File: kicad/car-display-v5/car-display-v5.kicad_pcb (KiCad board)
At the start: 4 copper layers, 35.8 x 35.8 mm, 52 parts, among them J1 AVRISP-6, J2 Screw_Terminal_01x03, J3 PicoBlade F 1x7, J4 Socket 1x6 0.1", J5 JMP 1x3 0.05", U1 ATmega328PB-M, U2 TXS0108ERGYR, U3 MCP25625T-E/ML, U4 TPSM365R3RDNR, U5 LP3988*-*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

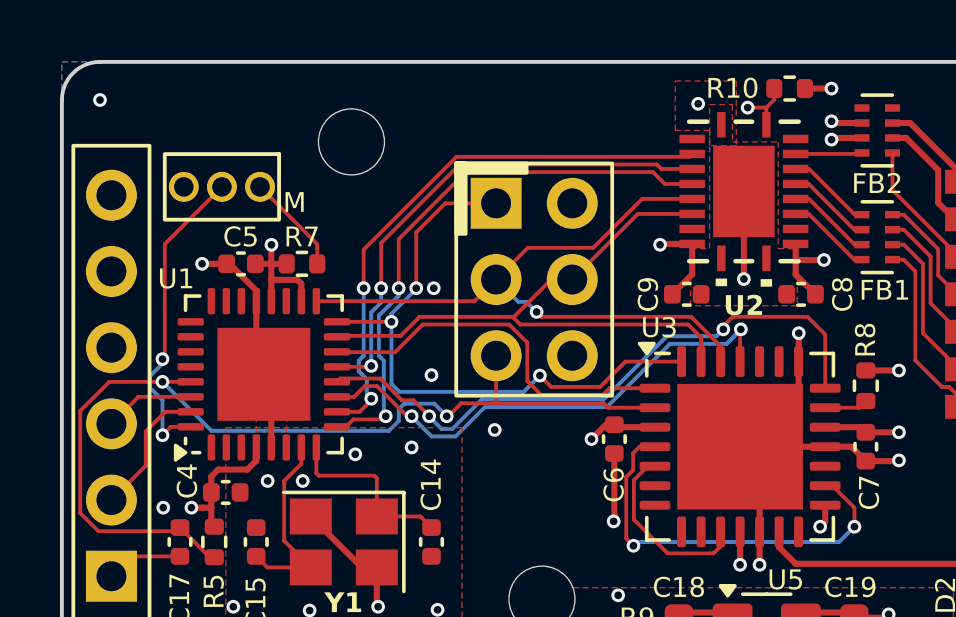
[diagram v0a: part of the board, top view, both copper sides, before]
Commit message: Add 3.3V PGOOD trace
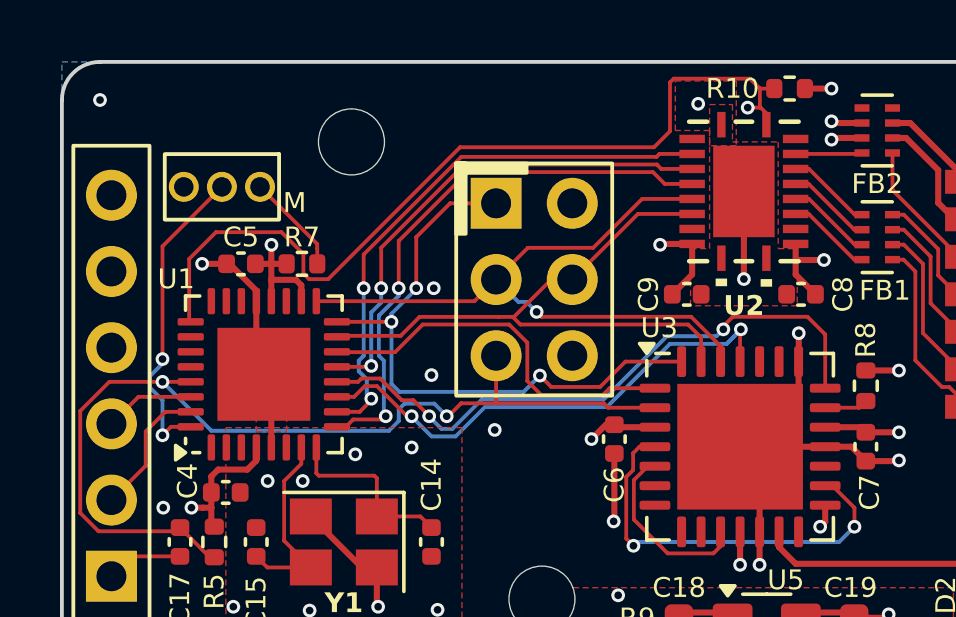
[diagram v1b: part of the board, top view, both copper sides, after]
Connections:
- U1 pad 25: unconnected-(U1-PC2-Pad25) -> PG_3V3
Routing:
- net PG_3V3: track 31.8 -> 58.4 mm

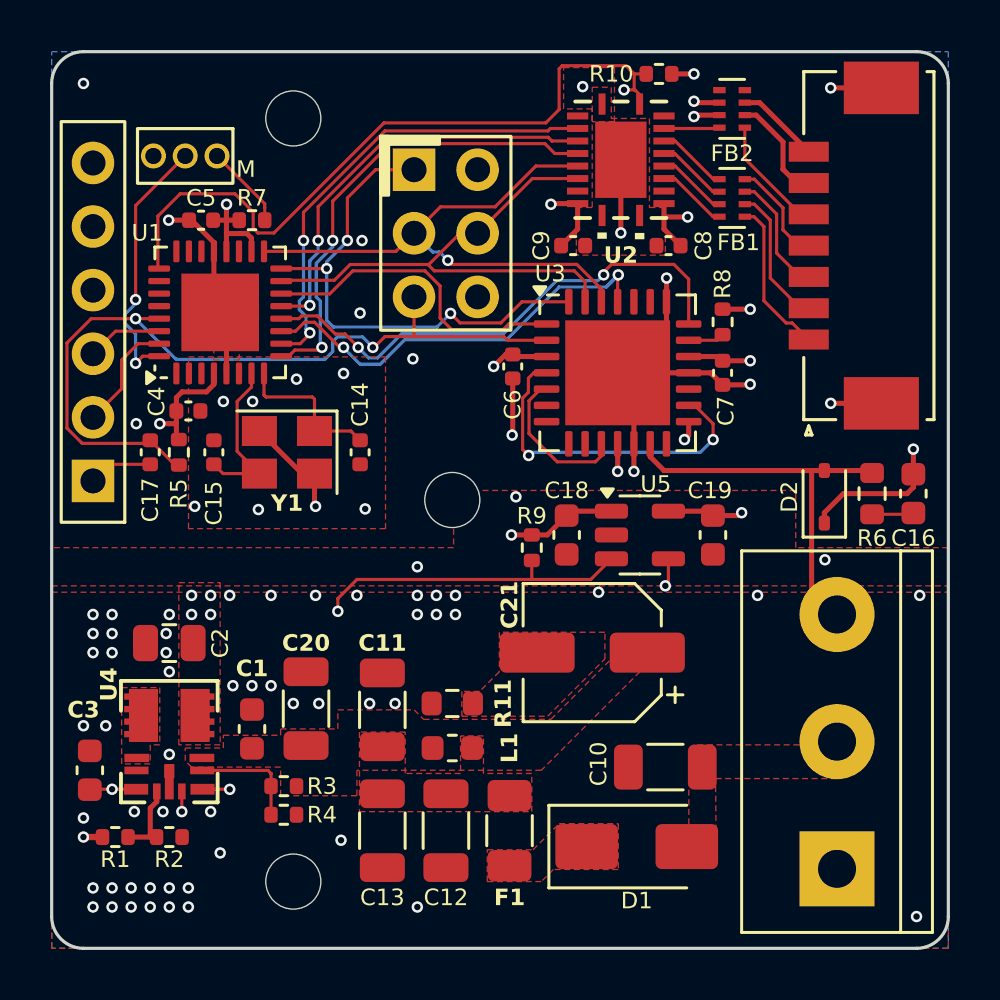
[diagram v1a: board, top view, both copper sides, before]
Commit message: Modify 3.3V trace
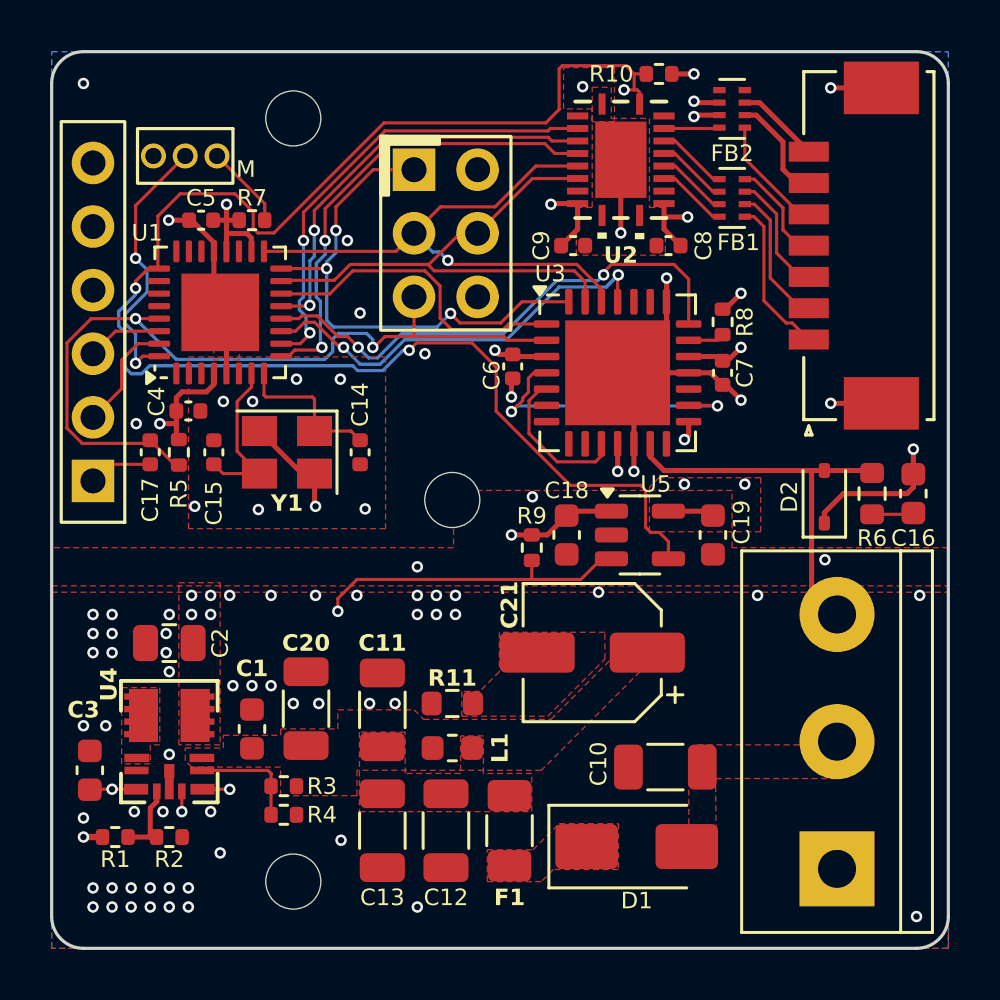
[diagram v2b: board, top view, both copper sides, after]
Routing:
- net PG_3V3: track 58.4 -> 62.0 mm, vias 2 -> 3
- net GND: track 43.9 -> 42.2 mm
- net T_{X}CAN: track 13.6 -> 11.9 mm
- net +3.3V: track 7.87 -> 6.67 mm, vias 4 -> 5
- added copper zone on F.Cu, net +3.3V

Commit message: Move OLED connector to side opposite of CAN input
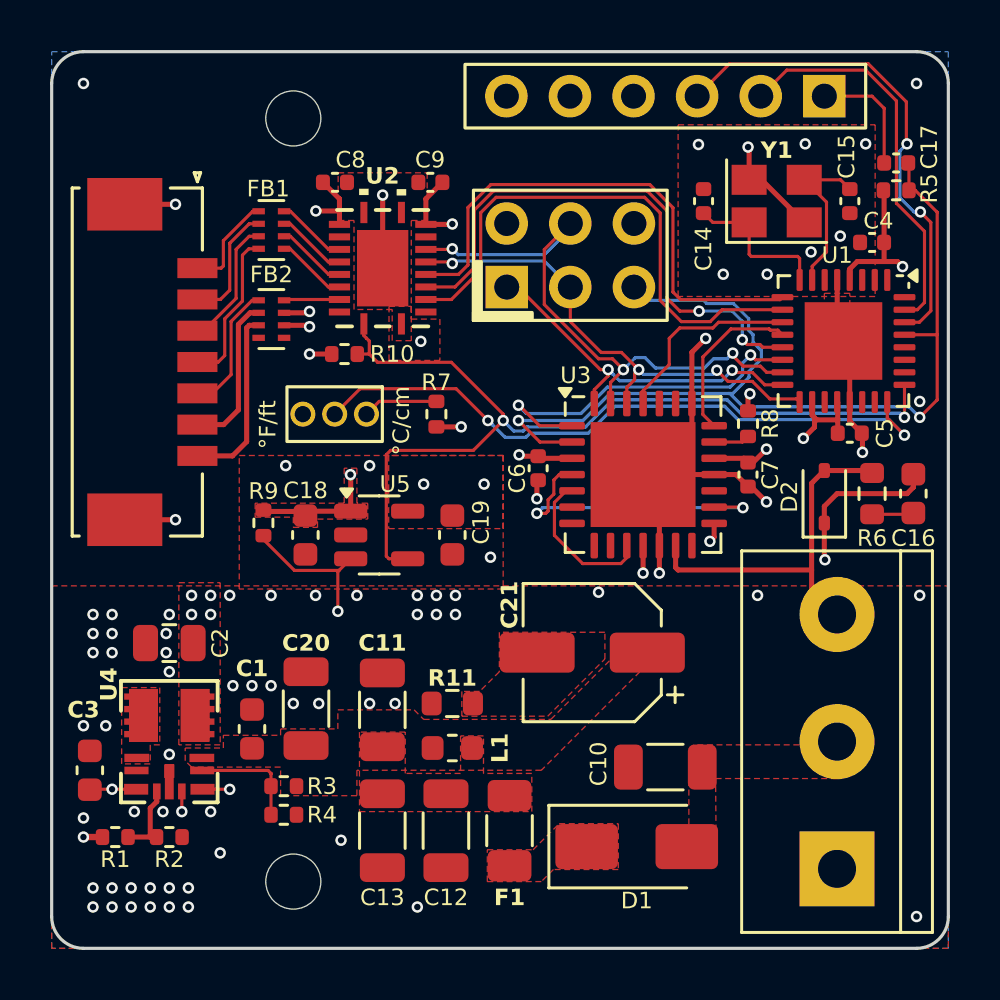
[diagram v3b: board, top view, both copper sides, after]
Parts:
- removed H3: MountingHole_Pad, MountingHole:MountingHole_2.2mm_M2_DIN965
- moved J4 33.0 mm to (143.6, 154.2), turned to -90 degrees
- moved C17 32.0 mm to (146.5, 156.8), turned to 180 degrees
- moved R5 30.5 mm to (146.5, 157.9), turned to 0 degrees
- moved C4 28.1 mm to (145.5, 160.0), turned to 180 degrees
- moved C15 27.3 mm to (144.7, 158.4), turned to -90 degrees
- moved C5 27.3 mm to (144.7, 167.6), turned to 0 degrees
- moved U1 24.9 mm to (144.4, 164.0), turned to -90 degrees
- moved J3 24.6 mm to (118.6, 161.0), turned to -90 degrees
- moved Y1 22.0 mm to (141.7, 158.4), turned to 0 degrees
- moved FB2 20.2 mm to (121.6, 163.1), turned to -90 degrees
- moved FB1 18.4 mm to (121.6, 159.5), turned to -90 degrees
- moved C14 17.0 mm to (138.8, 158.4), turned to 90 degrees
- moved R10 16.8 mm to (124.5, 164.5), turned to 0 degrees
- moved C8 13.6 mm to (124.1, 157.6), turned to 0 degrees
- moved J5 11.9 mm to (124.1, 166.9)
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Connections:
- net /OSC+ renamed OSC+
- net /OSC- renamed OSC-
- U1 pad 24: unconnected-(U1-PC1-Pad24) -> SEL_UNIT
- U1 pad 32: SEL_UNIT -> unconnected-(U1-PD2-Pad32)
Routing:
- net PG_3V3: track 62.0 -> 36.9 mm, vias 3 -> 2
- net FTDI_RX: track 3.02 -> 19.9 mm, vias 0 -> 2
- net SEL_UNIT: track 10.9 -> 26.6 mm
- net CLK: track 20.7 -> 6.67 mm, vias 2 -> 0
- net FTDI_TX: track 4.53 -> 15.8 mm
- net INT_CAN: track 17.5 -> 7.82 mm, vias 2 -> 0
- net RESET: track 32.7 -> 40.6 mm
- net PG_5V: track 23.5 -> 16.9 mm
- net MISO: track 20.7 -> 14.6 mm, vias 3 -> 2
- net RST_OLED: track 16.8 -> 22.2 mm
- net /3F_3.3V: track 3.36 -> 7.27 mm
- net SCK: track 22.9 -> 19.8 mm, vias 1 -> 3
- net CS_OLED: track 18.7 -> 21.6 mm, vias 2 -> 0
- net MOSI: track 20.9 -> 23.3 mm, vias 0 -> 3
- net /3F_MOSI: track 6.32 -> 3.98 mm
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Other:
- board text added: "°C/cm"
- board text added: "°F/ft"
- board text removed: "M"

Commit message: Updates
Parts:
- moved R10 8.62 mm to (130.2, 170.9), turned to -90 degrees
- moved FB2 1.14 mm to (121.7, 164.2)
- moved C17 0.93 mm to (147.2, 156.2)
- moved FB1 0.88 mm to (121.7, 160.4)
- moved R5 0.87 mm to (147.2, 157.4)
- moved J5 0.13 mm to (124.1, 167.0)
- turned C16 to -90 degrees
- turned D2 to -90 degrees
- turned R6 to -90 degrees
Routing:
- net GND: track 44.1 -> 42.1 mm, vias 80 -> 84
- net CANH: track 14.7 -> 12.9 mm
- net FTDI_TX: track 15.8 -> 14.2 mm
- net FTDI_RX: track 19.9 -> 18.7 mm, vias 2 -> 0
- net /3F_CS_OLED: track 5.23 -> 4.15 mm
- net /3F_3.3V: track 7.27 -> 6.19 mm
- net /3F_GND: track 6.30 -> 5.21 mm
- net +3.3V: track 4.82 -> 3.80 mm, vias 5 -> 7
- net /3F_MOSI: track 3.98 -> 3.14 mm
- net /3F_SCK: track 4.79 -> 3.96 mm
- net /3F_OLED_DC: track 5.16 -> 4.40 mm
- net /3F_OLED_RST: track 6.25 -> 5.57 mm
- net INT_CAN: track 7.82 -> 7.21 mm
- net /FTDI_RESET: track 4.77 -> 4.26 mm
- net PG_3V3: track 36.9 -> 36.3 mm
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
